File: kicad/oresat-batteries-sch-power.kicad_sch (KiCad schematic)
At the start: 89 parts, among them Q1 DMP2240UDM-7, Q2 PMV45ENR, Q3 DMP3050LVTQ-7, Q4 DMP3050LVTQ-7, Q44 PMV45ENR, Q5 PMV45ENR, U1 MAX7310, U2 MIC842LYC5, U3 MIC842LYC5, U4 MAX4211, U5 TPS62111RSA, U6 TS5A21366DCUR

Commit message: Not sure what changed from back in February, but committing anyway :)
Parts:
- C1, C2, C4: DIS Digi-Key -> DigiKey; DPN 1276-6524-1-ND -> 490-GRT188R71E105KE13DCT-ND; MFR Samsung -> Murata Electronics; MPN CL10B105MO8NNWC -> GRT188R71E105KE13D
- C12: DIS (none) -> DigiKey; DPN (none) -> 399-12983-1-ND; MFR (none) -> KEMET; MPN (none) -> C0603C103J5RACAUTO
- C13: DIS (none) -> DigiKey; DPN (none) -> 399-6820-1-ND; MFR (none) -> KEMET; MPN (none) -> C0603C473K5RACAUTO
- C14, C3, C37, C9: DIS Digi-Key -> DigiKey; DPN 399-1099-1-ND -> 399-6856-1-ND; MFR Samsung -> KEMET; MPN CL05B104KO5NNNC -> C0603C104K5RACAUTO
- C5: DIS Digi-Key -> DigiKey; DPN 1276-2893-1-ND -> 490-GRT21BC71E106KE13KCT-ND; MFR Samsung -> Murata Electronics; MPN CL21A106KOFNNNE -> GRT21BC71E106KE13K
- C6: DIS Digi-Key -> DigiKey; DPN 311-1446-1-ND -> 490-GRT188R71E105KE13DCT-ND; MFR Yageo -> Murata Electronics; MPN CC0603KRX7R7BB105 -> GRT188R71E105KE13D
- C7: DIS (none) -> DigiKey; DPN (none) -> 490-GRT188R71E105KE13DCT-ND; MFR (none) -> Murata Electronics; MPN (none) -> GRT188R71E105KE13D
- C8: DIS Digi-Key -> DigiKey; DPN 490-10511-1-ND -> 478-KAM21AT70J226KUCT-ND; MFR Murata -> KYOCERA AVX; MPN GRM21BR61A226ME51L -> KAM21AT70J226KU
- D1: DIS Digi-Key -> DigiKey; DPN 1830-1064-1-ND -> 732-4971-1-ND; MFR Inolux -> Wurth; MPN IN-S63AT5A -> 150060GS75000
- D2, D3: DIS Digi-Key -> DigiKey; DPN 511-1584-1-ND -> 732-4971-1-ND; MFR Rohm -> Wurth; MPN SML-E12M8WT86 -> 150060GS75000
- L1, U2, U5: DIS Digi-Key -> DigiKey
- R1: DPN 311-10.0HRCT-ND -> RMCF0603FT10R0CT-ND; MFR Yageo -> Stackpole Electronics; MPN RC0603FR-0710RL -> RMCF0603FT10R0
- R11, R17, R5: value 1K -> 1k; DPN 311-665KHRCT-ND -> RMCF0603FT2K70CT-ND; MFR Yageo -> Stackpole Electronics; MPN RC0603FR-07665KL -> RMCF0603FT1K00
- R12, R13: DPN 311-665KHRCT-ND -> RMCF0603FT665KCT-ND; MFR Yageo -> Stackpole Electronics; MPN RC0603FR-07665KL -> RMCF0603FT665K
- R18, R24, R25, R31, R32, R37, R38, R44: DIS Digi-Key -> DigiKey; DPN 311-10.0KHRCT-ND -> RMCF0603FT10K0CT-ND; MFR Yageo -> Stackpole Electronics; MPN RC0603FR-0710KL -> RMCF0603FT10K0
- R19, R20: DIS Digi-Key -> DigiKey; DPN A129718CT-ND -> RMCF0603FT330KCT-ND; MFR TE -> Stackpole Electronics; MPN CRGCQ0603F330K -> RMCF0603FT330K
- R21, R22: DIS Digi-Key -> DigiKey; DPN 311-1.00MHRCT-ND -> RMCF0603FT1M00CT-ND; MFR Yageo -> Stackpole Electronics; MPN RC0603FR-071ML -> RMCF0603FT1M00
- R23, R36, R39: DIS Digi-Key -> DigiKey; DPN A129693CT-ND -> RMCF0603FT2K70CT-ND; MFR TE -> Stackpole Electronics; MPN CRGCQ0603F2K7 -> RMCF0603FT2K70
- R26: DIS Digi-Key -> DigiKey; DPN 1276-4275-1-ND -> RMCF0603FT100KCT-ND; MFR Samsung -> Stackpole Electronics; MPN RC1005F6653CS -> RMCF0603FT100K
- R27, R98: DIS Digi-Key -> DigiKey; DPN 1276-4275-1-ND -> RMCF0603FT10K0CT-ND; MFR Samsung -> Stackpole Electronics; MPN RC1005F6653CS -> RMCF0603FT10K0
- R29: value NP -> 10k; DIS Digi-Key -> DigiKey; DPN 1276-4275-1-ND -> RMCF0603FT10K0CT-ND; MFR Samsung -> Stackpole Electronics; MPN RC1005F6653CS -> RMCF0603FT10K0
- R30: DIS Digi-Key -> DigiKey; DPN CSR1206FTR100CT-ND -> CSR1206FKR100CT-ND; MFR Stackpole -> Stackpole Electronics; MPN CSR1206FTR100 -> CSR1206FKR100
- R33: DIS Digi-Key -> DigiKey; DPN 311-0.0GRCT-ND -> RMCF0603ZT0R00CT-ND; MFR Yageo -> Stackpole Electronics; MPN RC0603JR-070RL -> RMCF0603ZT0R00
- R34: DIS Digi-Key -> DigiKey; DPN RR08P20.0KDCT-ND -> RMCF0603FT20K0CT-ND; MFR Samsung -> Stackpole Electronics; MPN RR0816P-203-D -> RMCF0603FT20K0
- R57, R67: DIS Digi-Key -> DigiKey; DPN 311-665KHRCT-ND -> RMCF0603FT10K0CT-ND; MFR Yageo -> Stackpole Electronics; MPN RC0603FR-07665KL -> RMCF0603FT10K0
- R6, R7: DPN 311-100HRCT-ND -> RMCF0603FT100RCT-ND; MFR Yageo -> Stackpole Electronics; MPN RC0603FR-07100RL -> RMCF0603FT100R
- R87: DIS (none) -> DigiKey; DPN (none) -> RMCF0603FT10K0CT-ND; MFR (none) -> Stackpole Electronics; MPN (none) -> RMCF0603FT10K0
- U1: DIS Digi-Key -> DigiKey; MFR Maxim -> Analog Devices; MPN MAX7310ATE -> MAX7310ATE+
- U3: DIS (none) -> DigiKey; DPN (none) -> 576-2927-1-ND; MFR (none) -> Microchip; MPN (none) -> MIC842LYC5-TR
- U4: DIS Digi-Key -> DigiKey; MFR Maxim -> Analog Devices
- U6: DIS (none) -> DigiKey; DPN (none) -> 296-24304-1-ND; MFR (none) -> Texas Instruments; MPN (none) -> TS5A21366DCUR
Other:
- note added: "Pulse skip for low power"

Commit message: Updated data, spiffed up the root page, renamed some STM specific OPD signals, synced SCH and BRD, fixed a bunch of DRC errors, NOW ready for MCXN import that will screw everything up.
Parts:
- removed TP4, TP6, TP7: TEST-POINT-LARGE-SQUARE, oresat-misc:TestPoint-0.75mm-th, symbol oresat-misc:Test-Point-0.75mm-th
- D1: value GRN -> AMB
- R10, R14, R15, R16, R2, R29, R3, R35, R4, R8, R9: footprint oresat-batteries:.0603-C-NOSILK -> oresat-passives:0603-C-NOSILK
- R57, R67: value 10k -> 1k
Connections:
- net ON/~{OFF}: now also C9.2, U6.8 (Vcc)
- net VPD: no longer C9.2, U6.8 (Vcc)
- net PA2/USART2_TX renamed MCU-UART-TX
- net PA3/USART2_RX renamed MCU-UART-RX
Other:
- note added: "ON/~{OFF} signal powers MAX4211 + TS5A Saves quiescent OPD power draw"
- moved on the sheet: C12, C13, C4, C5, C6, C7, C8, C9, D1, D2, D3, L1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

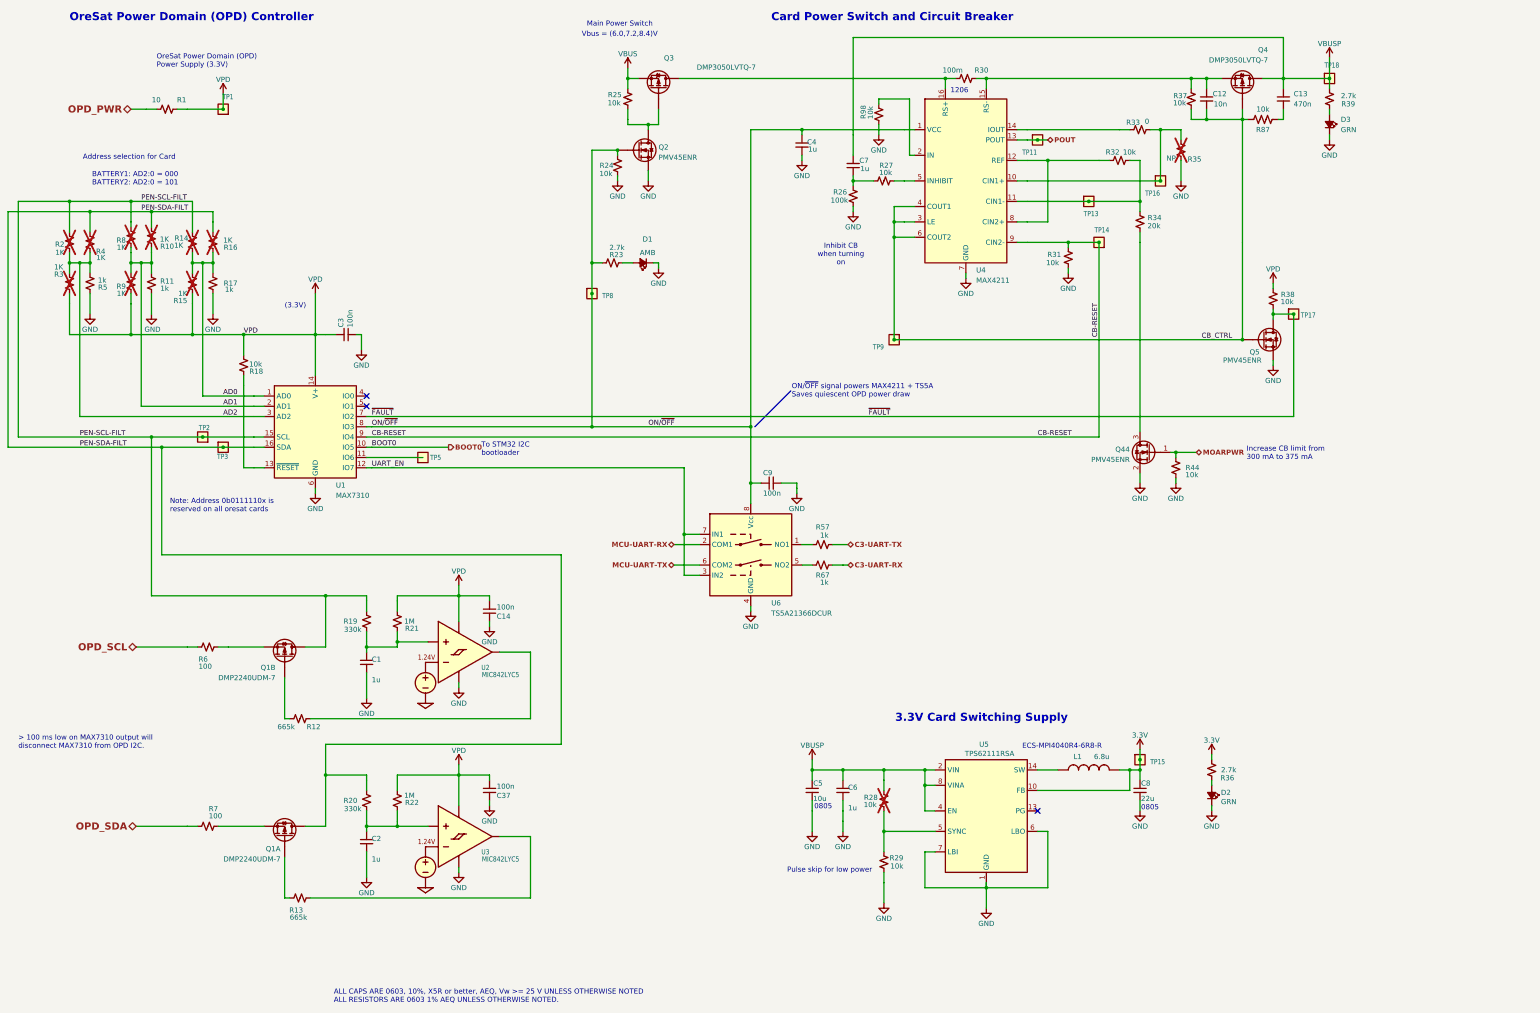
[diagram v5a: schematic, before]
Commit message: Added MCXN. Preliminary power layout, started removal of old symbols and footprints.
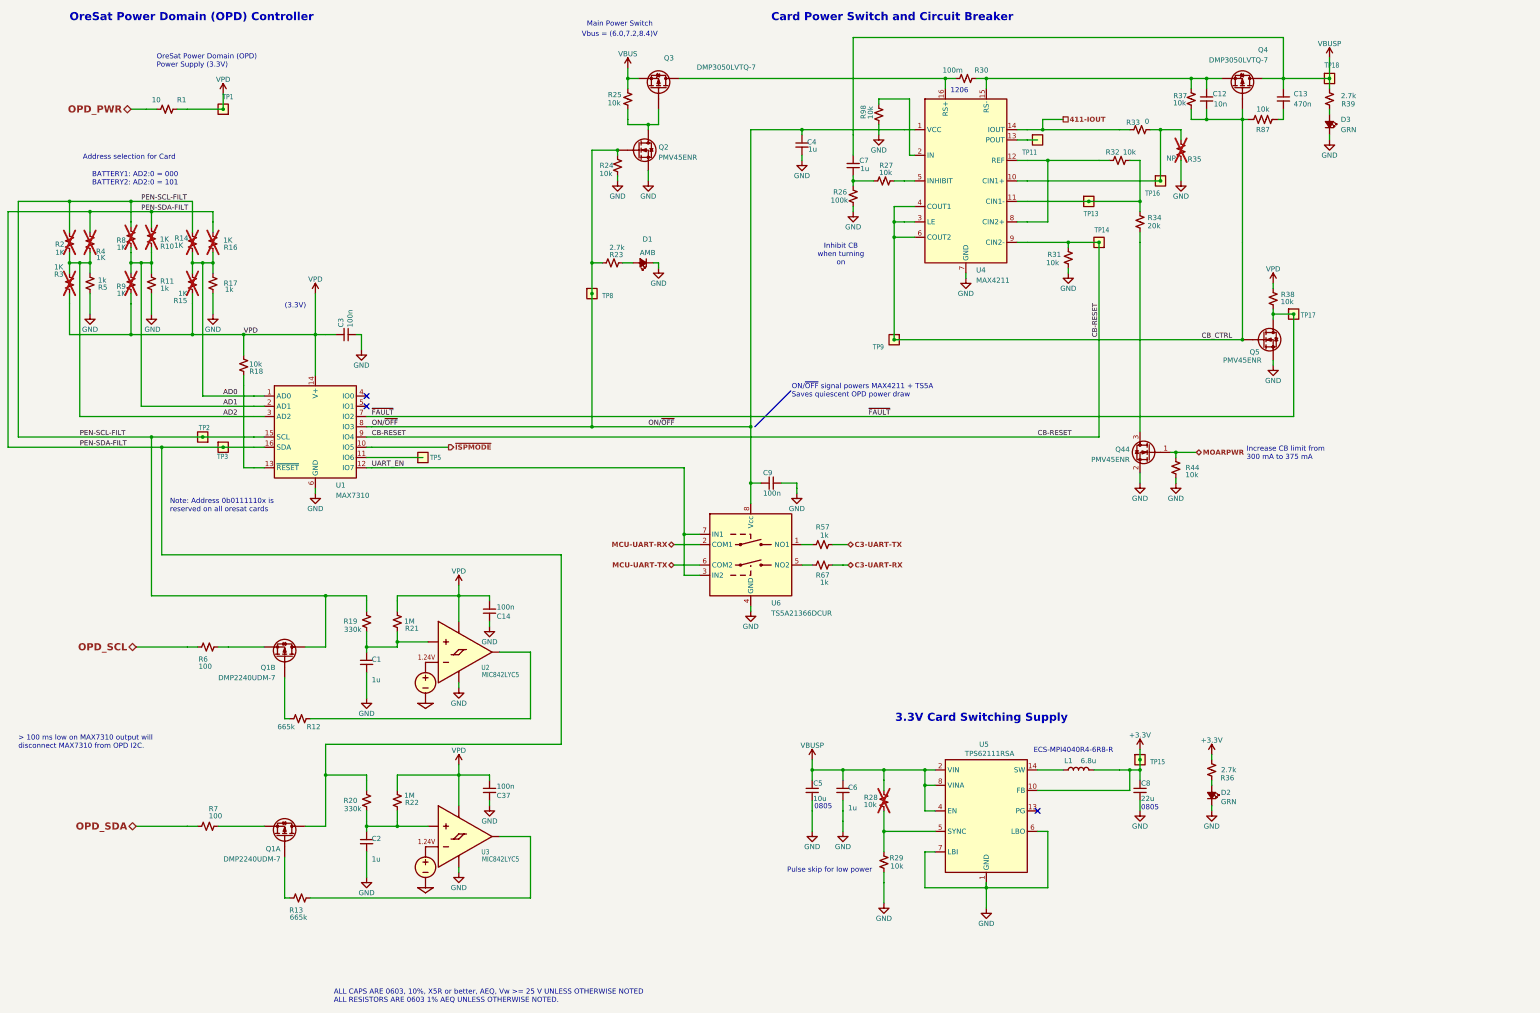
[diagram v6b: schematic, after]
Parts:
- L1: symbol oresat-batteries-eagle-import:L-ECS-MPI4040 -> Device:L
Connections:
- net 411-IOUT: now reaches R33.2, U4.14 (IOUT)
- net 3.3V renamed +3.3V
- net BOOT0 renamed ~{ISPMODE}
- net POUT: no longer names the net of TP11.1, U4.13 (POUT)
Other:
- note removed: "To STM32 I2C bootloader"

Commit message: Intermediary state on v4. Added one of two efuses.
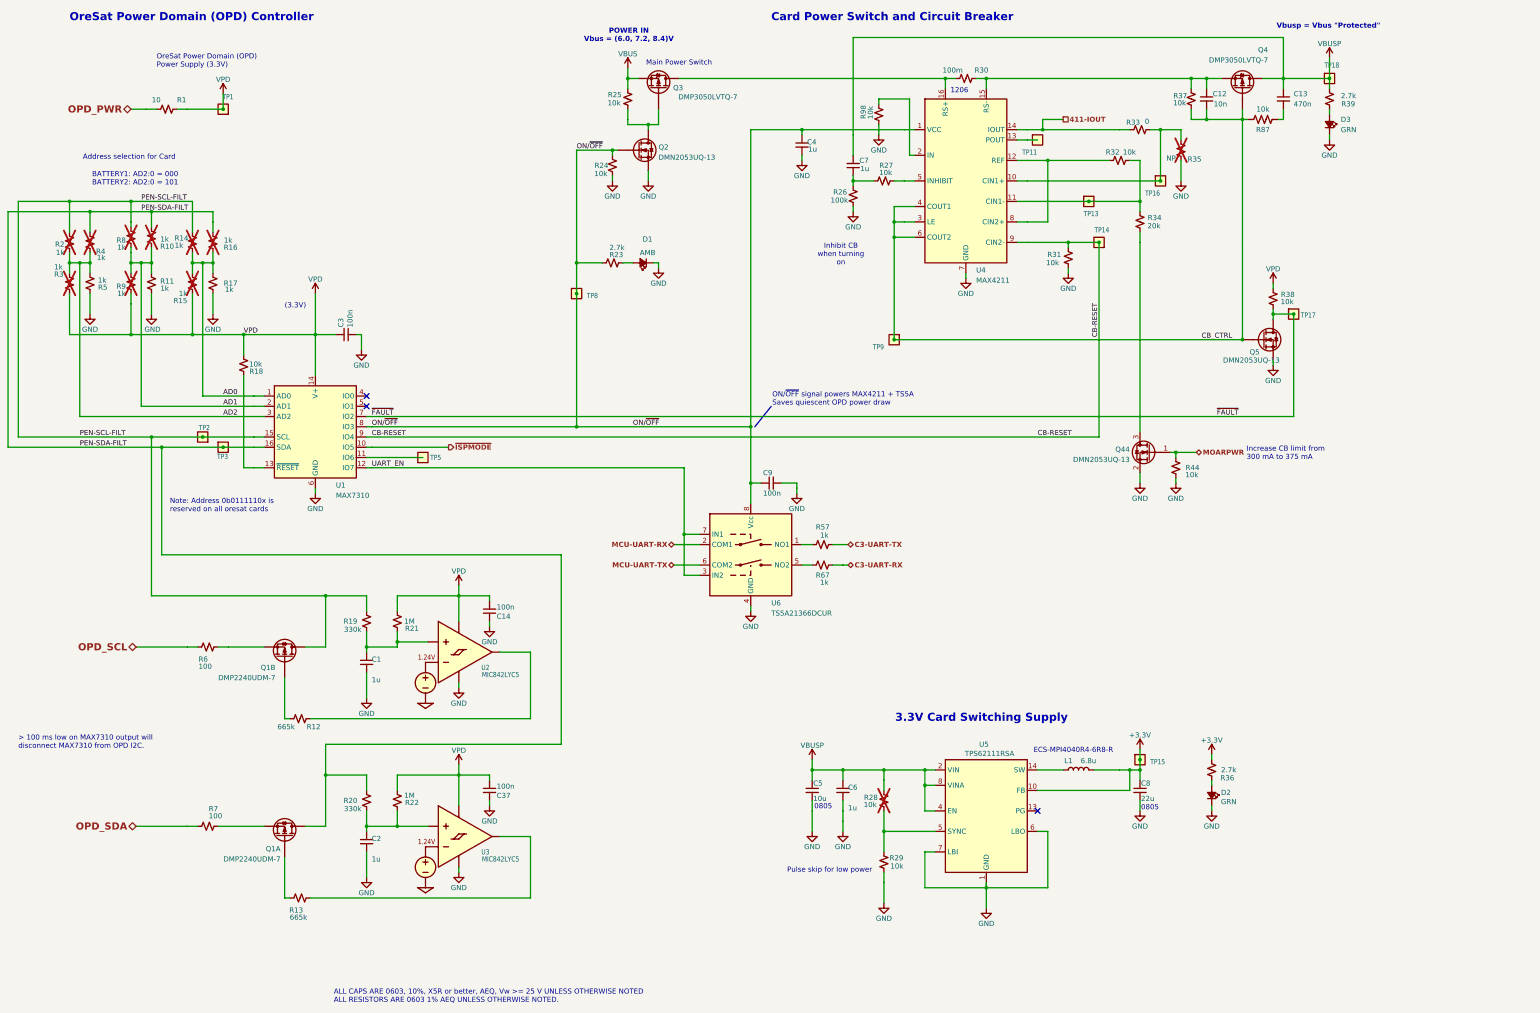
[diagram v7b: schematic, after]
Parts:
- C8: DPN 478-KAM21AT70J226KUCT-ND -> 490-GRT21BC81C226ME13LCT-ND; MFR KYOCERA AVX -> Murata Electronics; MPN KAM21AT70J226KU -> GRT21BC81C226ME13L
- D1: DPN 732-4971-1-ND -> 732-150060AS75000CT-ND; MPN 150060GS75000 -> 150060AS75000
- Q2, Q44, Q5: value PMV45ENR -> DMN2053UQ-13; DPN 1727-2307-1-ND -> 31-DMN2053UQ-13CT-ND; MFR Nexperia -> Diodes Incorporated; MPN PMV45EN2R -> DMN2053UQ-13
- Q3, Q4: MFR Diodes Inc -> Diodes Incorporated
- R10, R14, R15, R16, R2, R3, R4, R8, R9: value 1K -> 1k; DIS Digi-Key -> DigiKey; DPN 311-665KHRCT-ND -> RMCF0603FT2K70CT-ND; MFR Yageo -> Stackpole Electronics; MPN RC0603FR-07665KL -> RMCF0603FT1K00
- R57, R67: DPN RMCF0603FT10K0CT-ND -> RMCF0603FT2K70CT-ND; MPN RMCF0603FT10K0 -> RMCF0603FT1K00
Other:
- note added: "POWER IN Vbus = (6.0, 7.2, 8.4)V"
- note added: "Vbusp = Vbus "Protected""
- note removed: "Vbus = (6.0,7.2,8.4)V"
- moved on the sheet: R24, TP8
